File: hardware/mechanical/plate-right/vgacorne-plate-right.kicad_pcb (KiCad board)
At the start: 2 copper layers, 138.8 x 98 mm, 0 parts

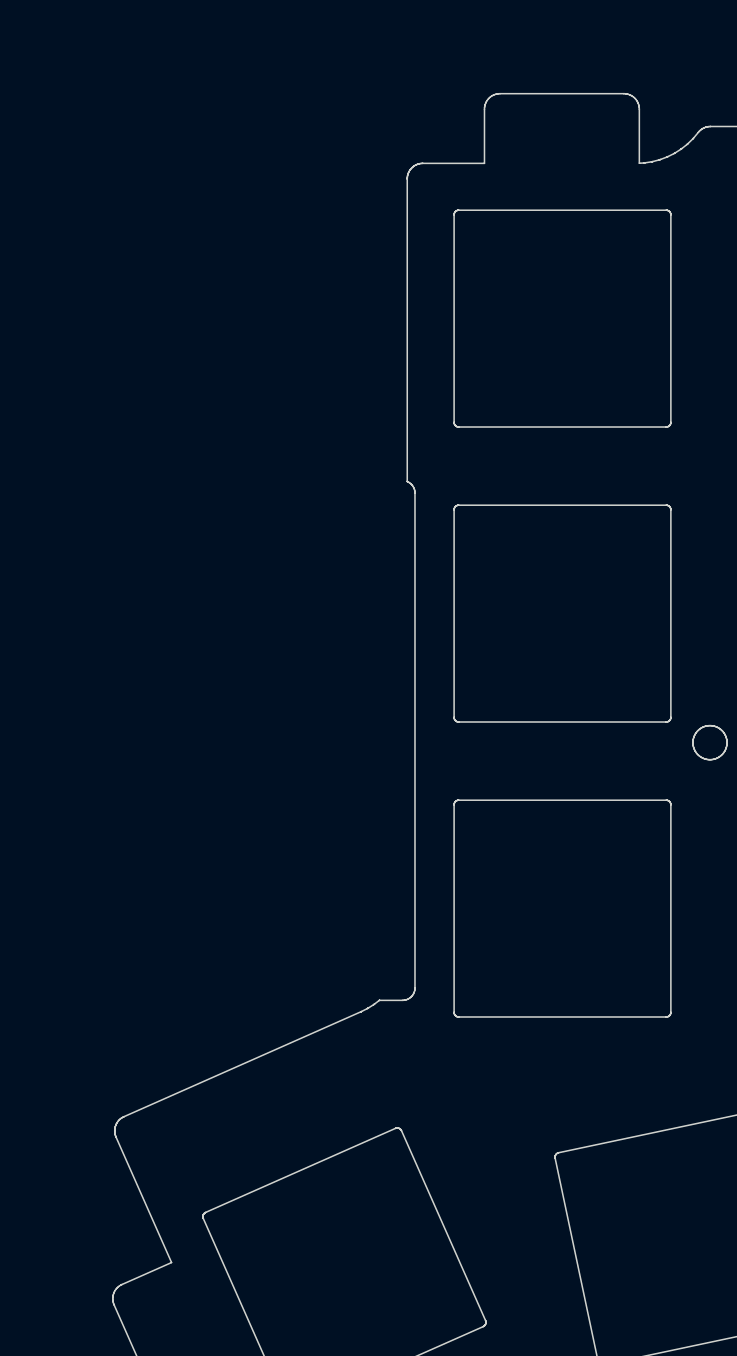
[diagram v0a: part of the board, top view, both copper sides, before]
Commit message: Add trackpad, mouse column and scroll wheel; move MCU and ports
Layout
- MCU module, USB-C and trackpad move to the right half; the left half
  is now the passive satellite.
- VGA daughterboard bay moves to the inner-back corner so both cables
  leave from the back face. The bay sits 4.5 mm further back than the
  keys need, so both halves are 116 mm deep.
- Azoteq TPS65 trackpad, landscape, right beside Y/H/N under a 1 mm
  overlay. The MCU module moves to a PCB ear behind it, next to the
  VGA bay. trackpad.py selects the pad (TPS65 or 40 mm Cirque); the
  case pocket, J5 connector and QMK driver follow the selection.
- Left half: a mouse column beside T/G/B with a scroll wheel (Bourns
  PEC12R) at the top and left/right-click HE keys beside G and B.

Circuits and firmware
- Mux channels reassigned so the satellite's mouse keys and wheel fill
  its three spare channels. The wheel's A/B contacts are summed into
  four voltage levels on one channel.
- QMK: 44-key LAYOUT and a wheel decoder that feeds QMK's quadrature
  encoder driver. Trackpad on I2C1, with rules.mk now generated. The
  host test covers the wheel.
- libhmk: MS_BTN1/MS_BTN2 on the mouse keys (no encoder support).

Case and renders
- Smoother milled case: 7.25 mm walls, 25 mm minimum outside radius
  and a flat back face at the ports.
- render.py builds Blender Cycles renders from the design geometry.

Co-Authored-By: Claude Opus 5.5 (1M context) <noreply@anthropic.com>
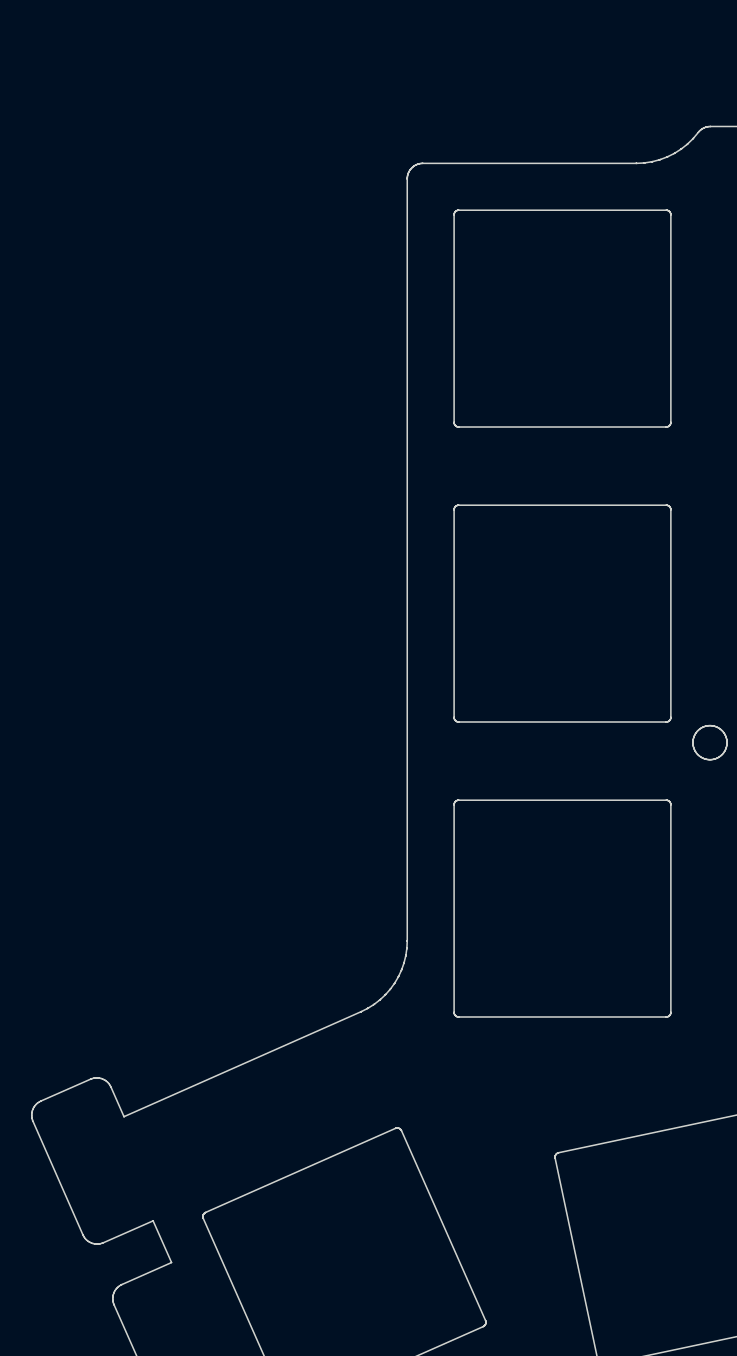
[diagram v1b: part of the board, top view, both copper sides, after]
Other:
- board size 138.8 x 98 mm -> 144 x 98 mm
